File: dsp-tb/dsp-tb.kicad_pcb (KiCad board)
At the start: 2 copper layers, 79 parts, among them J1 Conn_01x03, J10 USB_C_Receptacle_USB2.0, J2 Conn_ARM_SWD_TagConnect_TC2030, J3 Conn_01x04, J4 Conn_01x04, J5 Conn_01x03, J6 Conn_01x03, J7 Conn_01x03, J8 Conn_01x03, J9 104031-0811, SW1 SW_MEC_5E, SW2 SW_SPDT, U1 STM32H723ZGTx, U10 FSUSB42UMX, U11 CS4270-CZZ, U12 TLV9301xDBV, U13 TLV9301xDBV, U14 TLV9301xDBV, U15 TLV9301xDBV, U2 TLV76733QWDRBxQ1, U3 NCP718BSNADJT1G, U4 NCP718BSNADJT1G, U5 D3V3XA4B10LP, U6 IS42S16800F-7BL-TR, U7 IS25LP080D-JNLE, U8 USB3318C-CP-TR, U9 ASDMB-xxxMHz

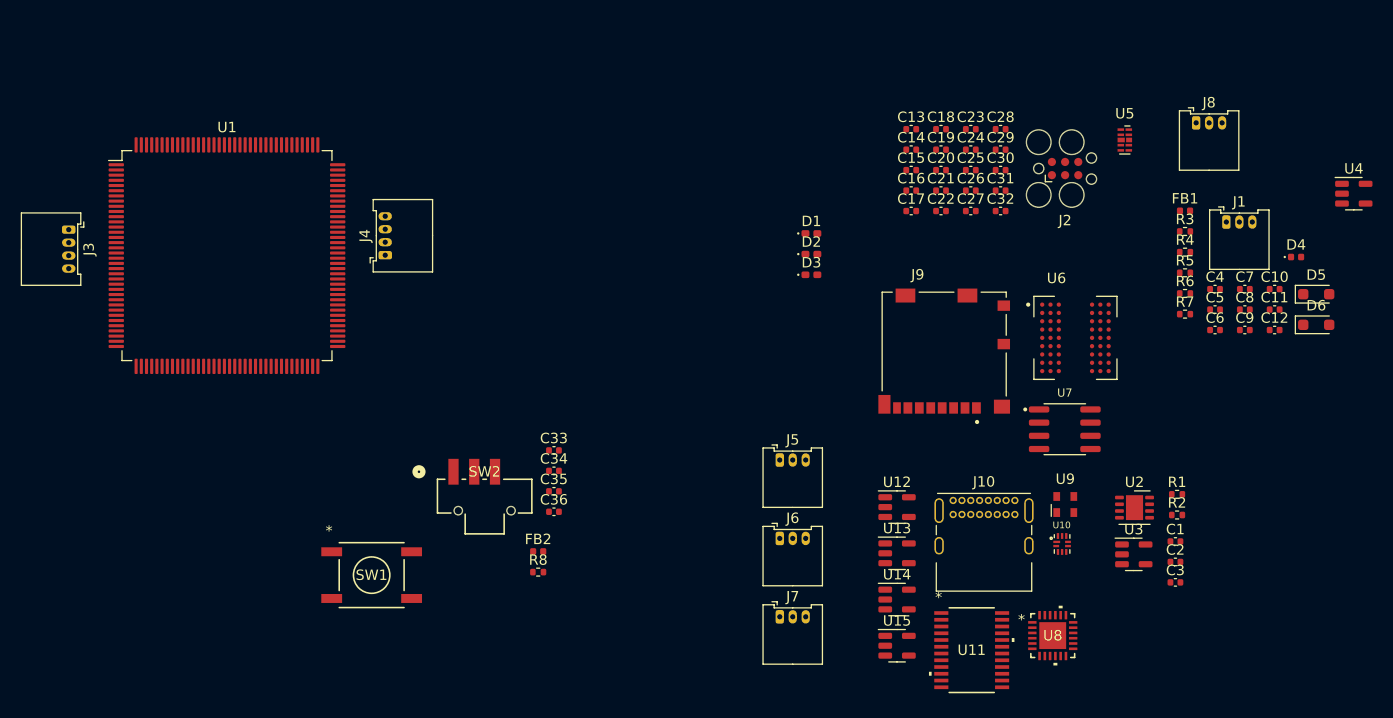
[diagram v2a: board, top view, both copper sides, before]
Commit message: dsp-tb: finish schematic drawings
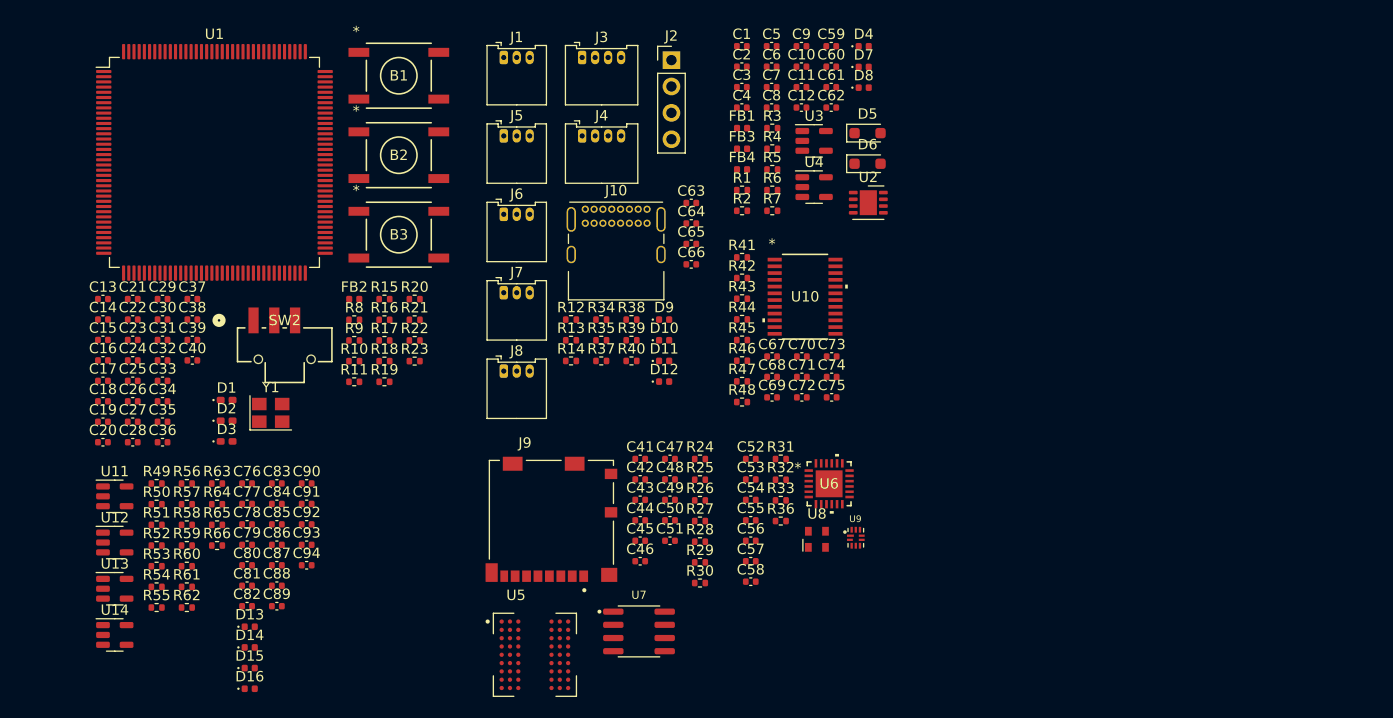
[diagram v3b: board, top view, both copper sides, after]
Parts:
- removed SW1: SW_MEC_5E, footprints:PTS645SL43SMTR92LFS_CNK
- removed U15: TLV9301xDBV, Package_TO_SOT_SMD:SOT-23-5
- added B1: SW_MEC_5E, footprints:PTS645SL43SMTR92LFS_CNK, F.Cu at (148.6, 66.5)
- added B2: SW_MEC_5E, footprints:PTS645SL43SMTR92LFS_CNK, F.Cu at (148.6, 74.1)
- added B3: SW_MEC_5E, footprints:PTS645SL43SMTR92LFS_CNK, F.Cu at (148.6, 81.8)
- added C37: 100n, Capacitor_SMD:C_0402_1005Metric, F.Cu at (128.7, 88.0)
- added C38: 100n, Capacitor_SMD:C_0402_1005Metric, F.Cu at (128.7, 90.0)
- added C39: 10p, Capacitor_SMD:C_0402_1005Metric, F.Cu at (128.7, 91.9)
- added C40: 10p, Capacitor_SMD:C_0402_1005Metric, F.Cu at (128.7, 93.9)
- added C41: 2u2, Capacitor_SMD:C_0402_1005Metric, F.Cu at (171.9, 103.4)
- added C42: 100n, Capacitor_SMD:C_0402_1005Metric, F.Cu at (171.9, 105.4)
- added C43: 100n, Capacitor_SMD:C_0402_1005Metric, F.Cu at (171.9, 107.3)
- added C44: 100n, Capacitor_SMD:C_0402_1005Metric, F.Cu at (171.9, 109.3)
- added C45: 2u2, Capacitor_SMD:C_0402_1005Metric, F.Cu at (171.9, 111.3)
- added C46: 100n, Capacitor_SMD:C_0402_1005Metric, F.Cu at (171.9, 113.3)
- added C47: 100n, Capacitor_SMD:C_0402_1005Metric, F.Cu at (174.7, 103.4)
- added C48: 100n, Capacitor_SMD:C_0402_1005Metric, F.Cu at (174.7, 105.4)
- added C49: 100n, Capacitor_SMD:C_0402_1005Metric, F.Cu at (174.7, 107.3)
- added C50: 2u2, Capacitor_SMD:C_0402_1005Metric, F.Cu at (174.7, 109.3)
- added C51: 2u2, Capacitor_SMD:C_0402_1005Metric, F.Cu at (174.7, 111.3)
- added C52: 2u2, Capacitor_SMD:C_0402_1005Metric, F.Cu at (182.5, 103.4)
- added C53: 2u2, Capacitor_SMD:C_0402_1005Metric, F.Cu at (182.5, 105.4)
- added C54: 100n, Capacitor_SMD:C_0402_1005Metric, F.Cu at (182.5, 107.3)
- added C55: 2u2, Capacitor_SMD:C_0402_1005Metric, F.Cu at (182.5, 109.3)
- added C56: 100n, Capacitor_SMD:C_0402_1005Metric, F.Cu at (182.5, 111.3)
- added C57: 100n, Capacitor_SMD:C_0402_1005Metric, F.Cu at (182.5, 113.3)
- added C58: 100n, Capacitor_SMD:C_0402_1005Metric, F.Cu at (182.5, 115.2)
- added C59: 100n, Capacitor_SMD:C_0402_1005Metric, F.Cu at (190.3, 63.7)
- added C60: 100n, Capacitor_SMD:C_0402_1005Metric, F.Cu at (190.3, 65.6)
- added C61: 100n, Capacitor_SMD:C_0402_1005Metric, F.Cu at (190.3, 67.6)
- added C62: 100n, Capacitor_SMD:C_0402_1005Metric, F.Cu at (190.3, 69.6)
- added C63: 10p, Capacitor_SMD:C_0402_1005Metric, F.Cu at (176.8, 78.8)
- added C64: 10p, Capacitor_SMD:C_0402_1005Metric, F.Cu at (176.8, 80.7)
- added C65: 10p, Capacitor_SMD:C_0402_1005Metric, F.Cu at (176.8, 82.7)
- added C66: 10p, Capacitor_SMD:C_0402_1005Metric, F.Cu at (176.8, 84.7)
- added C67: 100n, Capacitor_SMD:C_0402_1005Metric, F.Cu at (184.6, 93.5)
- added C68: 2u2, Capacitor_SMD:C_0402_1005Metric, F.Cu at (184.6, 95.5)
- added C69: 100n, Capacitor_SMD:C_0402_1005Metric, F.Cu at (184.6, 97.5)
- added C70: 100n, Capacitor_SMD:C_0402_1005Metric, F.Cu at (187.4, 93.5)
- added C71: 47u, Capacitor_SMD:C_0402_1005Metric, F.Cu at (187.4, 95.5)
- added C72: 47u, Capacitor_SMD:C_0402_1005Metric, F.Cu at (187.4, 97.5)
- added C73: 100n, Capacitor_SMD:C_0402_1005Metric, F.Cu at (190.3, 93.5)
- added C74: 100n, Capacitor_SMD:C_0402_1005Metric, F.Cu at (190.3, 95.5)
- added C75: 47u, Capacitor_SMD:C_0402_1005Metric, F.Cu at (190.3, 97.5)
- added C76: 220p, Capacitor_SMD:C_0402_1005Metric, F.Cu at (134.0, 105.8)
- added C77: 10n, Capacitor_SMD:C_0402_1005Metric, F.Cu at (134.0, 107.7)
- added C78: 100n, Capacitor_SMD:C_0402_1005Metric, F.Cu at (134.0, 109.7)
- added C79: 220p, Capacitor_SMD:C_0402_1005Metric, F.Cu at (134.0, 111.7)
- added C80: 10n, Capacitor_SMD:C_0402_1005Metric, F.Cu at (134.0, 113.6)
- added C81: 220p, Capacitor_SMD:C_0402_1005Metric, F.Cu at (134.0, 115.6)
- added C82: 10n, Capacitor_SMD:C_0402_1005Metric, F.Cu at (134.0, 117.6)
- added C83: 100n, Capacitor_SMD:C_0402_1005Metric, F.Cu at (136.9, 105.8)
- added C84: 220p, Capacitor_SMD:C_0402_1005Metric, F.Cu at (136.9, 107.7)
- added C85: 10n, Capacitor_SMD:C_0402_1005Metric, F.Cu at (136.9, 109.7)
- added C86: 47u, Capacitor_SMD:C_0402_1005Metric, F.Cu at (136.9, 111.7)
- added C87: 10n, Capacitor_SMD:C_0402_1005Metric, F.Cu at (136.9, 113.6)
- added C88: 1n, Capacitor_SMD:C_0402_1005Metric, F.Cu at (136.9, 115.6)
- added C89: 100n, Capacitor_SMD:C_0402_1005Metric, F.Cu at (136.9, 117.6)
- added C90: 10n, Capacitor_SMD:C_0402_1005Metric, F.Cu at (139.8, 105.8)
- added C91: 10n, Capacitor_SMD:C_0402_1005Metric, F.Cu at (139.8, 107.7)
- added C92: 1n, Capacitor_SMD:C_0402_1005Metric, F.Cu at (139.8, 109.7)
- added C93: 100n, Capacitor_SMD:C_0402_1005Metric, F.Cu at (139.8, 111.7)
- added C94: 10n, Capacitor_SMD:C_0402_1005Metric, F.Cu at (139.8, 113.6)
- added D10: CG0402MLU-12G, Diode_SMD:D_0402_1005Metric, F.Cu at (174.2, 92.0)
- added D11: CG0402MLU-12G, Diode_SMD:D_0402_1005Metric, F.Cu at (174.2, 94.0)
- added D12: CG0402MLU-12G, Diode_SMD:D_0402_1005Metric, F.Cu at (174.2, 96.0)
- added D13: CG0402MLU-12G, Diode_SMD:D_0402_1005Metric, F.Cu at (134.3, 119.6)
- added D14: CG0402MLU-12G, Diode_SMD:D_0402_1005Metric, F.Cu at (134.3, 121.6)
- added D15: CG0402MLU-12G, Diode_SMD:D_0402_1005Metric, F.Cu at (134.3, 123.5)
- added D16: CG0402MLU-12G, Diode_SMD:D_0402_1005Metric, F.Cu at (134.3, 125.5)
- added D7: CG0402MLU-12G, Diode_SMD:D_0402_1005Metric, F.Cu at (193.4, 65.7)
- added D8: CG0402MLU-12G, Diode_SMD:D_0402_1005Metric, F.Cu at (193.4, 67.6)
- added D9: CG0402MLU-12G, Diode_SMD:D_0402_1005Metric, F.Cu at (174.2, 90.0)
- added FB3: 120R@100MHz, Inductor_SMD:L_0402_1005Metric, F.Cu at (181.7, 73.5)
- added FB4: 120R@100MHz, Inductor_SMD:L_0402_1005Metric, F.Cu at (181.7, 75.5)
- added R10: 330, Resistor_SMD:R_0402_1005Metric, F.Cu at (144.3, 94.0)
- added R11: 330, Resistor_SMD:R_0402_1005Metric, F.Cu at (144.3, 96.0)
- added R12: 33, Resistor_SMD:R_0402_1005Metric, F.Cu at (165.2, 90.0)
- added R13: 33, Resistor_SMD:R_0402_1005Metric, F.Cu at (165.2, 92.0)
- added R14: 33, Resistor_SMD:R_0402_1005Metric, F.Cu at (165.2, 94.0)
- added R15: 4k7, Resistor_SMD:R_0402_1005Metric, F.Cu at (147.2, 88.0)
- added R16: 4k7, Resistor_SMD:R_0402_1005Metric, F.Cu at (147.2, 90.0)
- added R17: 33, Resistor_SMD:R_0402_1005Metric, F.Cu at (147.2, 92.0)
- added R18: 33, Resistor_SMD:R_0402_1005Metric, F.Cu at (147.2, 94.0)
- added R19: 33, Resistor_SMD:R_0402_1005Metric, F.Cu at (147.2, 96.0)
- added R20: 33, Resistor_SMD:R_0402_1005Metric, F.Cu at (150.2, 88.0)
- added R21: 33, Resistor_SMD:R_0402_1005Metric, F.Cu at (150.2, 90.0)
- added R22: 0, Resistor_SMD:R_0402_1005Metric, F.Cu at (150.2, 92.0)
- added R23: 33, Resistor_SMD:R_0402_1005Metric, F.Cu at (150.2, 94.0)
- added R24: 47k, Resistor_SMD:R_0402_1005Metric, F.Cu at (177.6, 103.4)
- added R25: 47k, Resistor_SMD:R_0402_1005Metric, F.Cu at (177.6, 105.4)
- added R26: 47k, Resistor_SMD:R_0402_1005Metric, F.Cu at (177.6, 107.4)
- added R27: 47k, Resistor_SMD:R_0402_1005Metric, F.Cu at (177.6, 109.4)
- added R28: 47k, Resistor_SMD:R_0402_1005Metric, F.Cu at (177.6, 111.4)
- added R29: 47k, Resistor_SMD:R_0402_1005Metric, F.Cu at (177.6, 113.4)
- added R30: 47k, Resistor_SMD:R_0402_1005Metric, F.Cu at (177.6, 115.4)
- added R31: 33, Resistor_SMD:R_0402_1005Metric, F.Cu at (185.4, 103.4)
- added R32: 5k1, Resistor_SMD:R_0402_1005Metric, F.Cu at (185.4, 105.4)
- added R33: 8k06, Resistor_SMD:R_0402_1005Metric, F.Cu at (185.4, 107.4)
- added R34: 5k1, Resistor_SMD:R_0402_1005Metric, F.Cu at (168.1, 90.0)
- added R35: 5k1, Resistor_SMD:R_0402_1005Metric, F.Cu at (168.1, 92.0)
- added R36: 5k1, Resistor_SMD:R_0402_1005Metric, F.Cu at (185.4, 109.4)
- added R37: 33, Resistor_SMD:R_0402_1005Metric, F.Cu at (168.1, 94.0)
- added R38: 33, Resistor_SMD:R_0402_1005Metric, F.Cu at (171.0, 90.0)
- added R39: 33, Resistor_SMD:R_0402_1005Metric, F.Cu at (171.0, 92.0)
- added R40: 33, Resistor_SMD:R_0402_1005Metric, F.Cu at (171.0, 94.0)
- added R41: 33, Resistor_SMD:R_0402_1005Metric, F.Cu at (181.7, 84.0)
- added R42: 2k2, Resistor_SMD:R_0402_1005Metric, F.Cu at (181.7, 86.0)
- added R43: 2k2, Resistor_SMD:R_0402_1005Metric, F.Cu at (181.7, 88.0)
- added R44: 10k, Resistor_SMD:R_0402_1005Metric, F.Cu at (181.7, 90.0)
- added R45: 10k, Resistor_SMD:R_0402_1005Metric, F.Cu at (181.7, 92.0)
- added R46: 10k, Resistor_SMD:R_0402_1005Metric, F.Cu at (181.7, 93.9)
- added R47: 10k, Resistor_SMD:R_0402_1005Metric, F.Cu at (181.7, 95.9)
- added R48: 47k, Resistor_SMD:R_0402_1005Metric, F.Cu at (181.7, 97.9)
- added R49: 100R, Resistor_SMD:R_0402_1005Metric, F.Cu at (125.3, 105.8)
- added R50: 1M, Resistor_SMD:R_0402_1005Metric, F.Cu at (125.3, 107.8)
- added R51: 1M, Resistor_SMD:R_0402_1005Metric, F.Cu at (125.3, 109.8)
- added R52: 1k, Resistor_SMD:R_0402_1005Metric, F.Cu at (125.3, 111.7)
- added R53: 100R, Resistor_SMD:R_0402_1005Metric, F.Cu at (125.3, 113.7)
- added R54: 1M, Resistor_SMD:R_0402_1005Metric, F.Cu at (125.3, 115.7)
- added R55: 1M, Resistor_SMD:R_0402_1005Metric, F.Cu at (125.3, 117.7)
- added R56: 1k, Resistor_SMD:R_0402_1005Metric, F.Cu at (128.2, 105.8)
- added R57: 1k, Resistor_SMD:R_0402_1005Metric, F.Cu at (128.2, 107.8)
- added R58: 1k, Resistor_SMD:R_0402_1005Metric, F.Cu at (128.2, 109.8)
- added R59: 1M, Resistor_SMD:R_0402_1005Metric, F.Cu at (128.2, 111.7)
- added R60: 1k, Resistor_SMD:R_0402_1005Metric, F.Cu at (128.2, 113.7)
- added R61: 100R, Resistor_SMD:R_0402_1005Metric, F.Cu at (128.2, 115.7)
- added R62: 1M, Resistor_SMD:R_0402_1005Metric, F.Cu at (128.2, 117.7)
- added R63: 1k, Resistor_SMD:R_0402_1005Metric, F.Cu at (131.1, 105.8)
- added R64: 100R, Resistor_SMD:R_0402_1005Metric, F.Cu at (131.1, 107.8)
- added R65: 10k, Resistor_SMD:R_0402_1005Metric, F.Cu at (131.1, 109.8)
- added R66: 10k, Resistor_SMD:R_0402_1005Metric, F.Cu at (131.1, 111.7)
- added R9: 330, Resistor_SMD:R_0402_1005Metric, F.Cu at (144.3, 92.0)
- added Y1: 403C11A24M, Crystal:Crystal_SMD_3225-4Pin_3.2x2.5mm, F.Cu at (136.3, 99.0)
- J2: value Conn_ARM_SWD_TagConnect_TC2030 -> Conn_01x04; footprint Connector:Tag-Connect_TC2030-IDC-FP_2x03_P1.27mm_Vertical -> Connector_PinHeader_2.54mm:PinHeader_1x04_P2.54mm_Vertical
- U10: value FSUSB42UMX -> CS4270-CZZ; footprint footprints:IC_FSUSB42UMX -> footprints:codec-cs4270
- U11: value CS4270-CZZ -> TLV9301xDBV; footprint footprints:codec-cs4270 -> Package_TO_SOT_SMD:SOT-23-5
- U5: value D3V3XA4B10LP -> IS42S16800F-7BLI; footprint Package_DFN_QFN:Diodes_UDFN-10_1.0x2.5mm_P0.5mm -> footprints:BGA54C80P9X9_800X800X120
- U6: value IS42S16800F-7BL-TR -> USB3318C-CP-TR; footprint footprints:BGA54C80P9X9_800X800X120 -> footprints:QFN24_4X4MC_MCH
- U8: value USB3318C-CP-TR -> ECS-2520MV-130-BN-TR; footprint footprints:QFN24_4X4MC_MCH -> Oscillator:Oscillator_SMD_Abracon_ASDMB-4Pin_2.5x2.0mm
- U9: value ASDMB-xxxMHz -> FSUSB42UMX; footprint Oscillator:Oscillator_SMD_Abracon_ASDMB-4Pin_2.5x2.0mm -> footprints:IC_FSUSB42UMX
- moved C28 88.9 mm to (123.0, 101.8)
- moved C18 84.9 mm to (120.1, 97.9)
- moved C19 84.9 mm to (120.1, 99.8)
- moved C20 84.9 mm to (120.1, 101.8)
- moved U11 83.8 mm to (121.3, 107.0)
- moved C23 83.2 mm to (123.0, 91.9)
- moved C24 83.2 mm to (123.0, 93.9)
- moved C25 83.2 mm to (123.0, 95.9)
- moved C26 83.2 mm to (123.0, 97.9)
- moved C27 83.2 mm to (123.0, 99.8)
- moved C29 82.0 mm to (125.9, 88.0)
- moved C30 82.0 mm to (125.9, 90.0)
- moved C31 82.0 mm to (125.9, 91.9)
- moved C32 82.0 mm to (125.9, 93.9)
- moved C13 79.5 mm to (120.1, 88.0)
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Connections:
- net Net-(J10-VBUS-PadA4) renamed VBUS
- net Net-(U1-BOOT0) renamed /MCU/MCU_BOOT0
- D1 pad 1: unconnected-(D1-K-Pad1) -> Net-(D1-K)
- D1 pad 2: unconnected-(D1-A-Pad2) -> GPIO_3V3_LED_R
- D2 pad 1: unconnected-(D2-K-Pad1) -> Net-(D2-K)
- D2 pad 2: unconnected-(D2-A-Pad2) -> GPIO_3V3_LED_Y
- D3 pad 1: unconnected-(D3-K-Pad1) -> Net-(D3-K)
- D3 pad 2: unconnected-(D3-A-Pad2) -> GPIO_3V3_LED_B
- D6 pad 2: VUSB_FILT -> Net-(D6-A)
- J1 pad 2: unconnected-(J1-Pin_2-Pad2) -> GND
- J10 pad A1: Net-(J10-GND-PadA1) -> GND
- J10 pad A12: Net-(J10-GND-PadA1) -> GND
- J10 pad A5: unconnected-(J10-CC1-PadA5) -> Net-(J10-CC1)
- J10 pad A6: unconnected-(J10-D+-PadA6) -> USB_D_P
- J10 pad A7: unconnected-(J10-D--PadA7) -> USB_D_N
- J10 pad B1: Net-(J10-GND-PadA1) -> GND
- J10 pad B12: Net-(J10-GND-PadA1) -> GND
- J10 pad B5: unconnected-(J10-CC2-PadB5) -> Net-(J10-CC2)
- J10 pad B6: unconnected-(J10-D+-PadB6) -> USB_D_P
- J10 pad B7: unconnected-(J10-D--PadB7) -> USB_D_N
- J2 pad 1: unconnected-(J2-VCC-Pad1) -> Net-(J2-Pin_1)
- J2 pad 2: unconnected-(J2-SWDIO-Pad2) -> Net-(J2-Pin_2)
- J2 pad 3: unconnected-(J2-~{RESET}-Pad3) -> Net-(J2-Pin_3)
- J2 pad 4: unconnected-(J2-SWCLK-Pad4) -> GND
- J3 pad 1: unconnected-(J3-Pin_1-Pad1) -> AUDIO_IN_L
- J3 pad 2: unconnected-(J3-Pin_2-Pad2) -> GND
- J3 pad 3: unconnected-(J3-Pin_3-Pad3) -> AUDIO_IN_R
- J3 pad 4: unconnected-(J3-Pin_4-Pad4) -> GND
- J4 pad 1: unconnected-(J4-Pin_1-Pad1) -> AUDIO_OUT_L
- J4 pad 2: unconnected-(J4-Pin_2-Pad2) -> GND
- J4 pad 3: unconnected-(J4-Pin_3-Pad3) -> AUDIO_OUT_R
- J4 pad 4: unconnected-(J4-Pin_4-Pad4) -> GND
- J5 pad 1: unconnected-(J5-Pin_1-Pad1) -> 3V3_ADC
- J5 pad 2: unconnected-(J5-Pin_2-Pad2) -> Net-(D9-K)
- J5 pad 3: unconnected-(J5-Pin_3-Pad3) -> GND
- J6 pad 1: unconnected-(J6-Pin_1-Pad1) -> 3V3_ADC
- J6 pad 2: unconnected-(J6-Pin_2-Pad2) -> Net-(D10-K)
- J6 pad 3: unconnected-(J6-Pin_3-Pad3) -> GND
- J7 pad 1: unconnected-(J7-Pin_1-Pad1) -> 3V3_ADC
- J7 pad 2: unconnected-(J7-Pin_2-Pad2) -> Net-(D11-K)
- J7 pad 3: unconnected-(J7-Pin_3-Pad3) -> GND
- J8 pad 1: unconnected-(J8-Pin_1-Pad1) -> 3V3_ADC
- J8 pad 2: unconnected-(J8-Pin_2-Pad2) -> Net-(D12-K)
- J8 pad 3: unconnected-(J8-Pin_3-Pad3) -> GND
- J9 pad 1: unconnected-(J9-DAT2-Pad1) -> SD_D2
- J9 pad 2: unconnected-(J9-CD/DAT3-Pad2) -> SD_D3
- J9 pad 3: unconnected-(J9-CMD-Pad3) -> SD_CMD
- J9 pad 4: unconnected-(J9-VDD-Pad4) -> +3V3
- J9 pad 5: unconnected-(J9-CLK-Pad5) -> SD_CLK
- J9 pad 6: unconnected-(J9-VSS-Pad6) -> GND
- J9 pad 7: unconnected-(J9-DAT0-Pad7) -> SD_D0
- J9 pad 8: unconnected-(J9-DAT1-Pad8) -> SD_D1
- J9 pad 9: unconnected-(J9-SW-1-Pad9) -> SD_DET
- J9 pad G1: Net-(J9-GND-PadG1) -> GND
- J9 pad G2: Net-(J9-GND-PadG1) -> GND
- J9 pad G3: Net-(J9-GND-PadG1) -> GND
- J9 pad G4: Net-(J9-GND-PadG1) -> GND
- U1 pad 1: unconnected-(U1-PE2-Pad1) -> /MCU/SAI1_MCLK_A
- U1 pad 10: unconnected-(U1-PF0-Pad10) -> RAM_A0
- U1 pad 102: unconnected-(U1-PA10-Pad102) -> USB_SW
- U1 pad 103: unconnected-(U1-PA11-Pad103) -> USB_FS_D_N
- U1 pad 104: unconnected-(U1-PA12-Pad104) -> USB_FS_D_P
- U1 pad 105: unconnected-(U1-PA13(JTMS-Pad105) -> MCU_SWDIO
- U1 pad 107: Net-(U1-VSS-Pad107) -> GND
- U1 pad 109: unconnected-(U1-PA14(JTCK-Pad109) -> MCU_SWCLK
- U1 pad 11: unconnected-(U1-PF1-Pad11) -> RAM_A1
- U1 pad 110: unconnected-(U1-PA15(JTDI)-Pad110) -> UART4_DE
- U1 pad 111: unconnected-(U1-PC10-Pad111) -> UART4_TX
- U1 pad 112: unconnected-(U1-PC11-Pad112) -> UART4_RX
- U1 pad 113: unconnected-(U1-PC12-Pad113) -> UART4_NRE
- U1 pad 114: unconnected-(U1-PD0-Pad114) -> RAM_D2
- U1 pad 115: unconnected-(U1-PD1-Pad115) -> RAM_D3
- U1 pad 12: unconnected-(U1-PF2-Pad12) -> RAM_A2
- U1 pad 120: Net-(U1-VSS-Pad107) -> GND
- U1 pad 122: unconnected-(U1-PD6-Pad122) -> SD_CLK
- U1 pad 123: unconnected-(U1-PD7-Pad123) -> SD_CMD
- U1 pad 124: unconnected-(U1-PG9-Pad124) -> SD_D0
- U1 pad 125: unconnected-(U1-PG10-Pad125) -> SD_D1
- U1 pad 126: unconnected-(U1-PG11-Pad126) -> SD_D2
- U1 pad 127: unconnected-(U1-PG12-Pad127) -> SD_D3
- U1 pad 128: unconnected-(U1-PG13-Pad128) -> SD_DET
- U1 pad 129: unconnected-(U1-PG14-Pad129) -> USB_NRST
- U1 pad 13: unconnected-(U1-PF3-Pad13) -> RAM_A3
- U1 pad 130: Net-(U1-VSS-Pad107) -> GND
- U1 pad 132: unconnected-(U1-PG15-Pad132) -> RAM_NCAS
- U1 pad 133: unconnected-(U1-PB3(JTDO-Pad133) -> MCU_SWO
- U1 pad 135: unconnected-(U1-PB5-Pad135) -> ULPI_D7
- U1 pad 14: unconnected-(U1-PF4-Pad14) -> RAM_A4
- U1 pad 141: unconnected-(U1-PE0-Pad141) -> RAM_DML
- U1 pad 142: unconnected-(U1-PE1-Pad142) -> RAM_DMH
- U1 pad 143: unconnected-(U1-PDR_ON-Pad143) -> /MCU/MCU_PDR_ON
- U1 pad 15: unconnected-(U1-PF5-Pad15) -> RAM_A5
- U1 pad 16: Net-(U1-VSS-Pad107) -> GND
- U1 pad 18: unconnected-(U1-PF6-Pad18) -> QSPI_IO3
- U1 pad 19: unconnected-(U1-PF7-Pad19) -> QSPI_IO2
- U1 pad 2: unconnected-(U1-PE3-Pad2) -> SAI1_SD_B
- U1 pad 20: unconnected-(U1-PF8-Pad20) -> QSPI_IO0
- U1 pad 21: unconnected-(U1-PF9-Pad21) -> QSPI_IO1
- U1 pad 22: unconnected-(U1-PF10-Pad22) -> /MCU/QSPI_CLK_R
- U1 pad 23: unconnected-(U1-PH0-Pad23) -> Net-(U1-PH0)
- U1 pad 24: unconnected-(U1-PH1-Pad24) -> Net-(U1-PH1)
- U1 pad 26: unconnected-(U1-PC0-Pad26) -> ULPI_STP
- U1 pad 28: unconnected-(U1-PC2_C-Pad28) -> ULPI_DIR
- U1 pad 29: unconnected-(U1-PC3_C-Pad29) -> ULPI_NXT
- U1 pad 3: unconnected-(U1-PE4-Pad3) -> /MCU/SAI1_FS_A
- U1 pad 31: unconnected-(U1-VSSA-Pad31) -> GND
- U1 pad 34: unconnected-(U1-PA0-Pad34) -> ADC_IN16
- U1 pad 35: unconnected-(U1-PA1-Pad35) -> ADC_IN17
- U1 pad 36: unconnected-(U1-PA2-Pad36) -> ADC_IN14
- U1 pad 37: unconnected-(U1-PA3-Pad37) -> ULPI_D0
- U1 pad 38: Net-(U1-VSS-Pad107) -> GND
- U1 pad 4: unconnected-(U1-PE5-Pad4) -> /MCU/SAI1_SCK_A
- U1 pad 40: unconnected-(U1-PA4-Pad40) -> ADC_IN18
- U1 pad 41: unconnected-(U1-PA5-Pad41) -> ULPI_CLK
- U1 pad 43: unconnected-(U1-PA7-Pad43) -> RAM_NWE
- U1 pad 44: unconnected-(U1-PC4-Pad44) -> RAM_NCS
- U1 pad 45: unconnected-(U1-PC5-Pad45) -> RAM_CKE
- U1 pad 46: unconnected-(U1-PB0-Pad46) -> ULPI_D1
- U1 pad 47: unconnected-(U1-PB1-Pad47) -> ULPI_D2
- U1 pad 49: unconnected-(U1-PF11-Pad49) -> RAM_NRAS
- U1 pad 5: unconnected-(U1-PE6-Pad5) -> /MCU/SAI1_SD_A
- U1 pad 50: unconnected-(U1-PF12-Pad50) -> RAM_A6
- U1 pad 51: Net-(U1-VSS-Pad107) -> GND
- U1 pad 53: unconnected-(U1-PF13-Pad53) -> RAM_A7
- U1 pad 54: unconnected-(U1-PF14-Pad54) -> RAM_A8
- U1 pad 55: unconnected-(U1-PF15-Pad55) -> RAM_A9
- U1 pad 56: unconnected-(U1-PG0-Pad56) -> RAM_A10
- U1 pad 57: unconnected-(U1-PG1-Pad57) -> RAM_A11
- U1 pad 58: unconnected-(U1-PE7-Pad58) -> RAM_D4
- U1 pad 59: unconnected-(U1-PE8-Pad59) -> RAM_D5
- U1 pad 60: unconnected-(U1-PE9-Pad60) -> RAM_D6
- U1 pad 61: Net-(U1-VSS-Pad107) -> GND
- U1 pad 63: unconnected-(U1-PE10-Pad63) -> RAM_D7
- U1 pad 64: unconnected-(U1-PE11-Pad64) -> RAM_D8
- U1 pad 65: unconnected-(U1-PE12-Pad65) -> RAM_D9
- U1 pad 66: unconnected-(U1-PE13-Pad66) -> RAM_D10
- U1 pad 67: unconnected-(U1-PE14-Pad67) -> RAM_D11
- U1 pad 68: unconnected-(U1-PE15-Pad68) -> RAM_D12
- U1 pad 69: unconnected-(U1-PB10-Pad69) -> ULPI_D3
- U1 pad 7: unconnected-(U1-PC13-Pad7) -> CODEC_NRST
- U1 pad 70: unconnected-(U1-PB11-Pad70) -> ULPI_D4
- U1 pad 73: unconnected-(U1-PB12-Pad73) -> ULPI_D5
- U1 pad 74: unconnected-(U1-PB13-Pad74) -> ULPI_D6
- U1 pad 77: unconnected-(U1-PD8-Pad77) -> RAM_D13
- U1 pad 78: unconnected-(U1-PD9-Pad78) -> RAM_D14
- U1 pad 79: unconnected-(U1-PD10-Pad79) -> RAM_D15
- U1 pad 81: unconnected-(U1-PD12-Pad81) -> I2C4_SCL
- U1 pad 82: unconnected-(U1-PD13-Pad82) -> I2C4_SDA
- U1 pad 83: Net-(U1-VSS-Pad107) -> GND
- U1 pad 85: unconnected-(U1-PD14-Pad85) -> RAM_D0
- U1 pad 86: unconnected-(U1-PD15-Pad86) -> RAM_D1
- U1 pad 89: unconnected-(U1-PG4-Pad89) -> RAM_BA0
- U1 pad 90: unconnected-(U1-PG5-Pad90) -> RAM_BA1
- U1 pad 91: unconnected-(U1-PG6-Pad91) -> QSPI_NCS
- U1 pad 93: unconnected-(U1-PG8-Pad93) -> /MCU/FMC_SDCLK
- U1 pad 94: Net-(U1-VSS-Pad107) -> GND
- U1 pad 97: unconnected-(U1-PC7-Pad97) -> GPIO_LED_R_3V3
- U1 pad 98: unconnected-(U1-PC8-Pad98) -> GPIO_LED_Y_3V3
- U1 pad 99: unconnected-(U1-PC9-Pad99) -> GPIO_LED_B_3V3
- U10 pad 1: unconnected-(U10-D+-Pad1) -> I2S_DAC_IN
- U10 pad 10: unconnected-(U10-SEL-Pad10) -> I2C4_SCL
- U10 pad 2: unconnected-(U10-D--Pad2) -> I2S_WCLK
- U10 pad 3: unconnected-(U10-GND-Pad3) -> I2S_MCLK
- U10 pad 4: unconnected-(U10-HSD1--Pad4) -> I2S_BCLK
- U10 pad 5: unconnected-(U10-HSD1+-Pad5) -> +3V3
- U10 pad 6: unconnected-(U10-HSD2--Pad6) -> GND
- U10 pad 7: unconnected-(U10-HSD2+-Pad7) -> Net-(U10-SDOUT)
- U10 pad 8: unconnected-(U10-~{OE}-Pad8) -> +3V3
- U10 pad 9: unconnected-(U10-VCC-Pad9) -> I2C4_SDA
- U11 pad 1: unconnected-(U11-SDIN-Pad1) -> Net-(U11--)
- U11 pad 2: unconnected-(U11-LRCK-Pad2) -> GND
- U11 pad 3: unconnected-(U11-MCLK-Pad3) -> Net-(U11-+)
- U11 pad 4: unconnected-(U11-SCLK-Pad4) -> Net-(U11--)
- U11 pad 5: unconnected-(U11-VD-Pad5) -> +5VA
- U12 pad 1: unconnected-(U12-Pad1) -> Net-(U12--)
- U12 pad 2: unconnected-(U12-V--Pad2) -> GND
- U12 pad 3: unconnected-(U12-+-Pad3) -> Net-(U12-+)
- U12 pad 4: unconnected-(U12---Pad4) -> Net-(U12--)
- U12 pad 5: unconnected-(U12-V+-Pad5) -> +5VA
- U13 pad 1: unconnected-(U13-Pad1) -> Net-(U13--)
- U13 pad 2: unconnected-(U13-V--Pad2) -> GND
- U13 pad 3: unconnected-(U13-+-Pad3) -> Net-(U13-+)
- U13 pad 4: unconnected-(U13---Pad4) -> Net-(U13--)
- U13 pad 5: unconnected-(U13-V+-Pad5) -> +5VA
- U14 pad 1: unconnected-(U14-Pad1) -> Net-(U14--)
- U14 pad 2: unconnected-(U14-V--Pad2) -> GND
- U14 pad 3: unconnected-(U14-+-Pad3) -> Net-(U14-+)
- U14 pad 4: unconnected-(U14---Pad4) -> Net-(U14--)
- U14 pad 5: unconnected-(U14-V+-Pad5) -> +5VA
- U7 pad 1: unconnected-(U7-CE#-Pad1) -> QSPI_NCS
- U7 pad 2: unconnected-(U7-SO(IO1)-Pad2) -> QSPI_IO0
- U7 pad 3: unconnected-(U7-WP#(IO2)-Pad3) -> QSPI_IO2
- U7 pad 4: unconnected-(U7-GND-Pad4) -> GND
- U7 pad 5: unconnected-(U7-SI(IO0)-Pad5) -> QSPI_IO1
- U7 pad 6: unconnected-(U7-SCK-Pad6) -> QSPI_CLK
- U7 pad 7: unconnected-(U7-HOLD/RESET-Pad7) -> QSPI_IO3
- U7 pad 8: unconnected-(U7-VCC-Pad8) -> +3V3
- U8 pad 1: unconnected-(U8-ID-Pad1) -> +3V3
- U8 pad 2: unconnected-(U8-VBUS-Pad2) -> GND
- U8 pad 3: unconnected-(U8-VBAT-Pad3) -> Net-(U8-Out)
- U8 pad 4: unconnected-(U8-VDD3.3-Pad4) -> +3V3
- U9 pad 1: unconnected-(U9-Standby-Pad1) -> USB_D_P
- U9 pad 2: unconnected-(U9-GND-Pad2) -> USB_D_N
- U9 pad 3: unconnected-(U9-Out-Pad3) -> GND
- U9 pad 4: unconnected-(U9-VDD-Pad4) -> USB_HS_D_N
